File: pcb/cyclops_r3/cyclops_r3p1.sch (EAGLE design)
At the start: 59 parts, among them Q1 SUM11006, Q2 IRF510, U1 MCP4921, U2 317-N, U3 ADR03, U4 OP1177, U5 LM324N, U6 ZXTD45

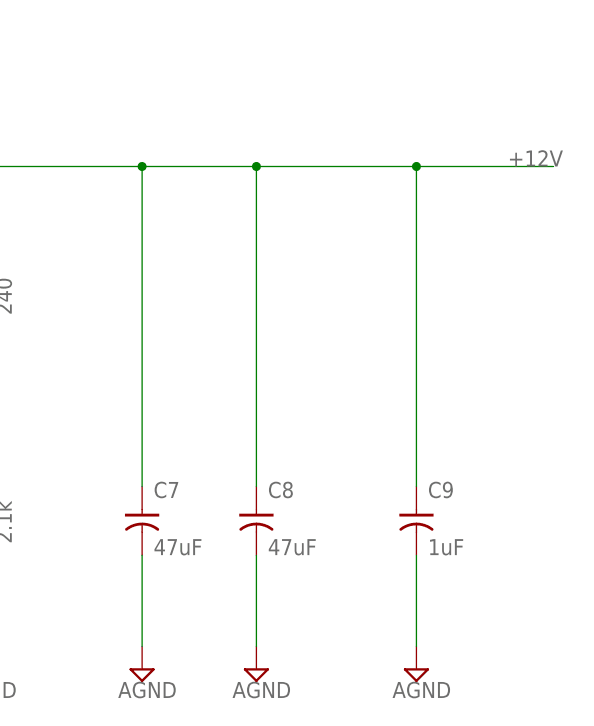
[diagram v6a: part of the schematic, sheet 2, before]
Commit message: Substantial changes to the layout of the analog frontend of the circuit.
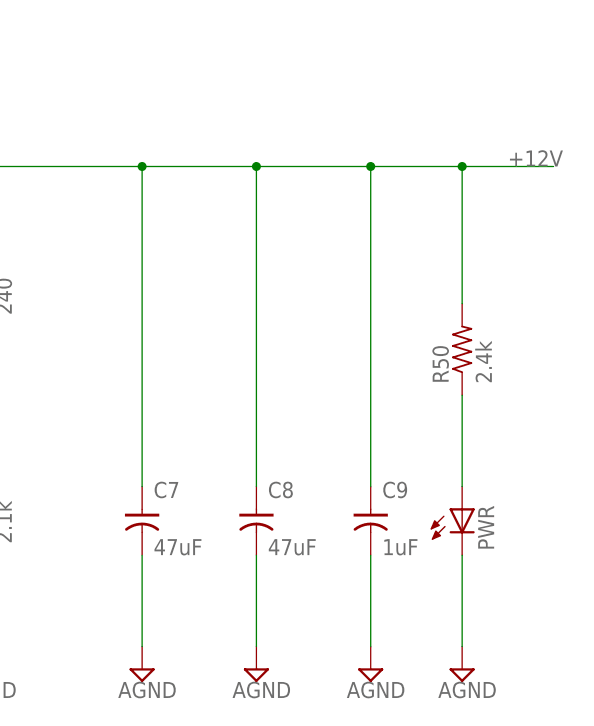
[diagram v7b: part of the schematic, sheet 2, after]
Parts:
- added PWR: (no value), cyclops:LEDYELLOW_0805
- added R50: 2.4k, cyclops:R_0603
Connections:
- net VREF2X renamed REFA2X
- new net N$3: PWR.A, R50.1
- new net REFA: C2.1, REF_ADJ.A, U1.REFA, U3.VOUT, U5A.+IN, VREF.TP
- net +12V: now also R50.2
- net GND: now also PWR.C
- net N$4: now also U5C.OUT; no longer U5A.OUT
- net N$8: now also U5A.-IN; no longer U5D.-IN
- net VFB: now also U5C.-IN; no longer U5A.-IN
- net VREF: now also U5D.-IN, U5D.OUT; no longer C2.1, REF_ADJ.A, U1.REFA, U3.VOUT, U5C.-IN, U5C.OUT, U5D.+IN, VREF.TP
- net VREFA2X: now also U5A.OUT; no longer U5D.OUT
- net _VREF: now also U5D.+IN; no longer U5A.+IN
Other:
- moved on the sheet: C9, U5A, U5C, U5D
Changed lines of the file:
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@@
 <part name="VBIAS" library="cyclops" deviceset="TP" device="TP08R"/>
 <part name="VGATE" library="cyclops" deviceset="TP" device="TP08R"/>
+<part name="R50" library="cyclops" deviceset="R" device="_0603" value="2.4k"/>
+<part name="PWR" library="cyclops" deviceset="LED" device="_0805" technology="YELLOW"/>
+<part name="SUPPLY40" library="supply2" deviceset="AGND" device=""/>
 </parts>
 <sheets>
@@
 </segment>
 </net>
-<net name="VREF" class="0">
-<segment>
-<pinref part="I/O_BLOCK" gate="G$1" pin="6"/>
-<wire x1="43.18" y1="-30.48" x2="68.58" y2="-30.48" width="0.1524" layer="91"/>
-<label x="50.8" y="-30.48" size="1.778" layer="95"/>
-</segment>
+<net name="REFA" class="0">
 <segment>
 <pinref part="U1" gate="G$1" pin="REFA"/>
@@
 </segment>
 </net>
-<net name="VREF2X" class="0">
+<net name="REFA2X" class="0">
 <segment>
 <pinref part="S3" gate="G$1" pin="3"/>
 <wire x1="119.38" y1="-27.94" x2="104.14" y2="-27.94" width="0.1524" layer="91"/>
 <label x="104.14" y="-27.94" size="1.778" layer="95"/>
+</segment>
+</net>
+<net name="VREF" class="0">
+<segment>
+<pinref part="I/O_BLOCK" gate="G$1" pin="6"/>
+<wire x1="43.18" y1="-30.48" x2="68.58" y2="-30.48" width="0.1524" layer="91"/>
+<label x="50.8" y="-30.48" size="1.778" layer="95"/>
 </segment>
 </net>
@@
 <instance part="SUPPLY8" gate="G$1" x="33.02" y="-58.42"/>
 <instance part="SUPPLY9" gate="G$1" x="86.36" y="-58.42"/>
-<instance part="SUPPLY10" gate="G$1" x="104.14" y="-58.42"/>
+<instance part="SUPPLY10" gate="G$1" x="99.06" y="-58.42"/>
 <instance part="C5" gate="C" x="12.7" y="-43.18"/>
 <instance part="C6" gate="C" x="33.02" y="-43.18"/>
-<instance part="C9" gate="C" x="104.14" y="-43.18"/>
+<instance part="C9" gate="C" x="99.06" y="-43.18"/>
 <instance part="C8" gate="C" x="86.36" y="-43.18"/>
 <instance part="SUPPLY11" gate="G$1" x="12.7" y="-58.42"/>
@@
 <instance part="C7" gate="C" x="73.66" y="-43.18"/>
 <instance part="SUPPLY31" gate="G$1" x="73.66" y="-58.42"/>
+<instance part="R50" gate="R" x="109.22" y="-22.86" rot="R90"/>
+<instance part="PWR" gate="G$1" x="109.22" y="-40.64"/>
+<instance part="SUPPLY40" gate="G$1" x="109.22" y="-58.42"/>
 </instances>
 <busses>
@@
 <wire x1="55.88" y1="-2.54" x2="73.66" y2="-2.54" width="0.1524" layer="91"/>
 <wire x1="73.66" y1="-2.54" x2="86.36" y2="-2.54" width="0.1524" layer="91"/>
-<wire x1="86.36" y1="-2.54" x2="104.14" y2="-2.54" width="0.1524" layer="91"/>
-<wire x1="104.14" y1="-2.54" x2="119.38" y2="-2.54" width="0.1524" layer="91"/>
+<wire x1="86.36" y1="-2.54" x2="99.06" y2="-2.54" width="0.1524" layer="91"/>
+<wire x1="99.06" y1="-2.54" x2="109.22" y2="-2.54" width="0.1524" layer="91"/>
+<wire x1="109.22" y1="-2.54" x2="119.38" y2="-2.54" width="0.1524" layer="91"/>
 <wire x1="38.1" y1="10.16" x2="55.88" y2="10.16" width="0.1524" layer="91"/>
 <wire x1="55.88" y1="10.16" x2="55.88" y2="-2.54" width="0.1524" layer="91"/>
@@
 <junction x="86.36" y="-2.54"/>
 <pinref part="C9" gate="C" pin="+"/>
-<wire x1="104.14" y1="-38.1" x2="104.14" y2="-2.54" width="0.1524" layer="91"/>
-<junction x="104.14" y="-2.54"/>
+<wire x1="99.06" y1="-38.1" x2="99.06" y2="-2.54" width="0.1524" layer="91"/>
+<junction x="99.06" y="-2.54"/>
 <label x="114.3" y="-2.54" size="1.778" layer="95"/>
 <pinref part="C7" gate="C" pin="+"/>
 <wire x1="73.66" y1="-38.1" x2="73.66" y2="-2.54" width="0.1524" layer="91"/>
 <junction x="73.66" y="-2.54"/>
+<pinref part="R50" gate="R" pin="2"/>
+<wire x1="109.22" y1="-17.78" x2="109.22" y2="-2.54" width="0.1524" layer="91"/>
+<junction x="109.22" y="-2.54"/>
 </segment>
 </net>
@@
 <pinref part="C9" gate="C" pin="-"/>
 <pinref part="SUPPLY10" gate="G$1" pin="AGND"/>
-<wire x1="104.14" y1="-45.72" x2="104.14" y2="-55.88" width="0.1524" layer="91"/>
+<wire x1="99.06" y1="-45.72" x2="99.06" y2="-55.88" width="0.1524" layer="91"/>
 </segment>
 <segment>
@@
 <wire x1="73.66" y1="-45.72" x2="73.66" y2="-55.88" width="0.1524" layer="91"/>
 <pinref part="SUPPLY31" gate="G$1" pin="AGND"/>
+</segment>
+<segment>
+<pinref part="PWR" gate="G$1" pin="C"/>
+<pinref part="SUPPLY40" gate="G$1" pin="AGND"/>
+<wire x1="109.22" y1="-45.72" x2="109.22" y2="-55.88" width="0.1524" layer="91"/>
 </segment>
 </net>
@@
 <wire x1="-10.16" y1="-15.24" x2="-10.16" y2="-2.54" width="0.1524" layer="91"/>
 <junction x="-10.16" y="-2.54"/>
+</segment>
+</net>
+<net name="N$3" class="0">
+<segment>
+<pinref part="R50" gate="R" pin="1"/>
+<wire x1="109.22" y1="-27.94" x2="109.22" y2="-38.1" width="0.1524" layer="91"/>
+<pinref part="PWR" gate="G$1" pin="A"/>
 </segment>
 </net>
@@
 </segment>
 </net>
-<net name="VREF" class="0">
+<net name="REFA" class="0">
 <segment>
 <wire x1="17.78" y1="2.54" x2="35.56" y2="2.54" width="0.1524" layer="91"/>
@@
 </plain>
 <instances>
-<instance part="U5" gate="A" x="27.94" y="83.82"/>
+<instance part="U5" gate="C" x="27.94" y="83.82"/>
 <instance part="U5" gate="B" x="27.94" y="22.86" rot="MR0"/>
-<instance part="U5" gate="C" x="-45.72" y="139.7" rot="MR0"/>
+<instance part="U5" gate="D" x="-45.72" y="139.7" rot="MR0"/>
 <instance part="U5" gate="P" x="27.94" y="83.82"/>
 <instance part="CTL_K" gate="1" x="-55.88" y="81.28" rot="MR90"/>
@@
 <instance part="R12" gate="R" x="134.62" y="71.12" rot="R90"/>
 <instance part="SUPPLY1" gate="G$1" x="134.62" y="45.72"/>
-<instance part="U5" gate="D" x="-53.34" y="-5.08"/>
+<instance part="U5" gate="A" x="-53.34" y="-5.08"/>
 <instance part="R13" gate="R" x="-40.64" y="-27.94" rot="R270"/>
 <instance part="R14" gate="R" x="-53.34" y="-15.24" rot="R180"/>
@@
 <wire x1="12.7" y1="81.28" x2="20.32" y2="81.28" width="0.1524" layer="91"/>
 <wire x1="12.7" y1="63.5" x2="12.7" y2="81.28" width="0.1524" layer="91"/>
-<pinref part="U5" gate="A" pin="-IN"/>
+<pinref part="U5" gate="C" pin="-IN"/>
 <pinref part="S4" gate="G$1" pin="2"/>
 </segment>
@@
 </segment>
 </net>
-<net name="VREF" class="0">
-<segment>
-<wire x1="-38.1" y1="137.16" x2="-38.1" y2="129.54" width="0.1524" layer="91"/>
-<wire x1="-38.1" y1="129.54" x2="-58.42" y2="129.54" width="0.1524" layer="91"/>
-<pinref part="U5" gate="C" pin="-IN"/>
-<wire x1="-73.66" y1="139.7" x2="-58.42" y2="139.7" width="0.1524" layer="91"/>
-<wire x1="-58.42" y1="139.7" x2="-53.34" y2="139.7" width="0.1524" layer="91"/>
-<wire x1="-58.42" y1="129.54" x2="-58.42" y2="139.7" width="0.1524" layer="91"/>
-<junction x="-58.42" y="139.7"/>
-<pinref part="U5" gate="C" pin="OUT"/>
-<label x="-73.66" y="139.7" size="1.778" layer="95"/>
-</segment>
-<segment>
-<pinref part="U5" gate="D" pin="+IN"/>
+<net name="REFA" class="0">
+<segment>
+<pinref part="U5" gate="A" pin="+IN"/>
 <wire x1="-73.66" y1="-2.54" x2="-60.96" y2="-2.54" width="0.1524" layer="91"/>
 <label x="-73.66" y="-2.54" size="1.778" layer="95"/>
@@
 <net name="_VREF" class="0">
 <segment>
-<pinref part="U5" gate="A" pin="+IN"/>
+<pinref part="U5" gate="C" pin="+IN"/>
 <pinref part="D4" gate="G$1" pin="C"/>
 <pinref part="R7" gate="R" pin="2"/>
@@
 <wire x1="-10.16" y1="86.36" x2="-10.16" y2="93.98" width="0.1524" layer="91"/>
 <wire x1="-20.32" y1="142.24" x2="-20.32" y2="86.36" width="0.1524" layer="91"/>
-<pinref part="U5" gate="C" pin="+IN"/>
+<pinref part="U5" gate="D" pin="+IN"/>
 <wire x1="-38.1" y1="142.24" x2="-20.32" y2="142.24" width="0.1524" layer="91"/>
 <junction x="-20.32" y="86.36"/>
@@
 <segment>
 <wire x1="-40.64" y1="-15.24" x2="-40.64" y2="-5.08" width="0.1524" layer="91"/>
-<pinref part="U5" gate="D" pin="OUT"/>
+<pinref part="U5" gate="A" pin="OUT"/>
 <wire x1="-40.64" y1="-5.08" x2="-45.72" y2="-5.08" width="0.1524" layer="91"/>
 <wire x1="-40.64" y1="-5.08" x2="-30.48" y2="-5.08" width="0.1524" layer="91"/>
@@
 <segment>
 <wire x1="-66.04" y1="-7.62" x2="-66.04" y2="-15.24" width="0.1524" layer="91"/>
-<pinref part="U5" gate="D" pin="-IN"/>
+<pinref part="U5" gate="A" pin="-IN"/>
 <wire x1="-60.96" y1="-7.62" x2="-66.04" y2="-7.62" width="0.1524" layer="91"/>
 <pinref part="R14" gate="R" pin="2"/>
@@
 </segment>
 </net>
-<net name="VREF2X" class="0">
+<net name="REFA2X" class="0">
 <segment>
 <pinref part="R15" gate="R" pin="2"/>
@@
 <net name="N$4" class="0">
 <segment>
-<pinref part="U5" gate="A" pin="OUT"/>
+<pinref part="U5" gate="C" pin="OUT"/>
 <wire x1="35.56" y1="83.82" x2="43.18" y2="83.82" width="0.1524" layer="91"/>
 <wire x1="43.18" y1="83.82" x2="43.18" y2="124.46" width="0.1524" layer="91"/>
@@
 </segment>
 </net>
+<net name="VREF" class="0">
+<segment>
+<wire x1="-38.1" y1="137.16" x2="-38.1" y2="129.54" width="0.1524" layer="91"/>
+<wire x1="-38.1" y1="129.54" x2="-58.42" y2="129.54" width="0.1524" layer="91"/>
+<pinref part="U5" gate="D" pin="-IN"/>
+<wire x1="-73.66" y1="139.7" x2="-58.42" y2="139.7" width="0.1524" layer="91"/>
+<wire x1="-58.42" y1="139.7" x2="-53.34" y2="139.7" width="0.1524" layer="91"/>
+<wire x1="-58.42" y1="129.54" x2="-58.42" y2="139.7" width="0.1524" layer="91"/>
+<junction x="-58.42" y="139.7"/>
+<pinref part="U5" gate="D" pin="OUT"/>
+<label x="-73.66" y="139.7" size="1.778" layer="95"/>
+</segment>
+</net>

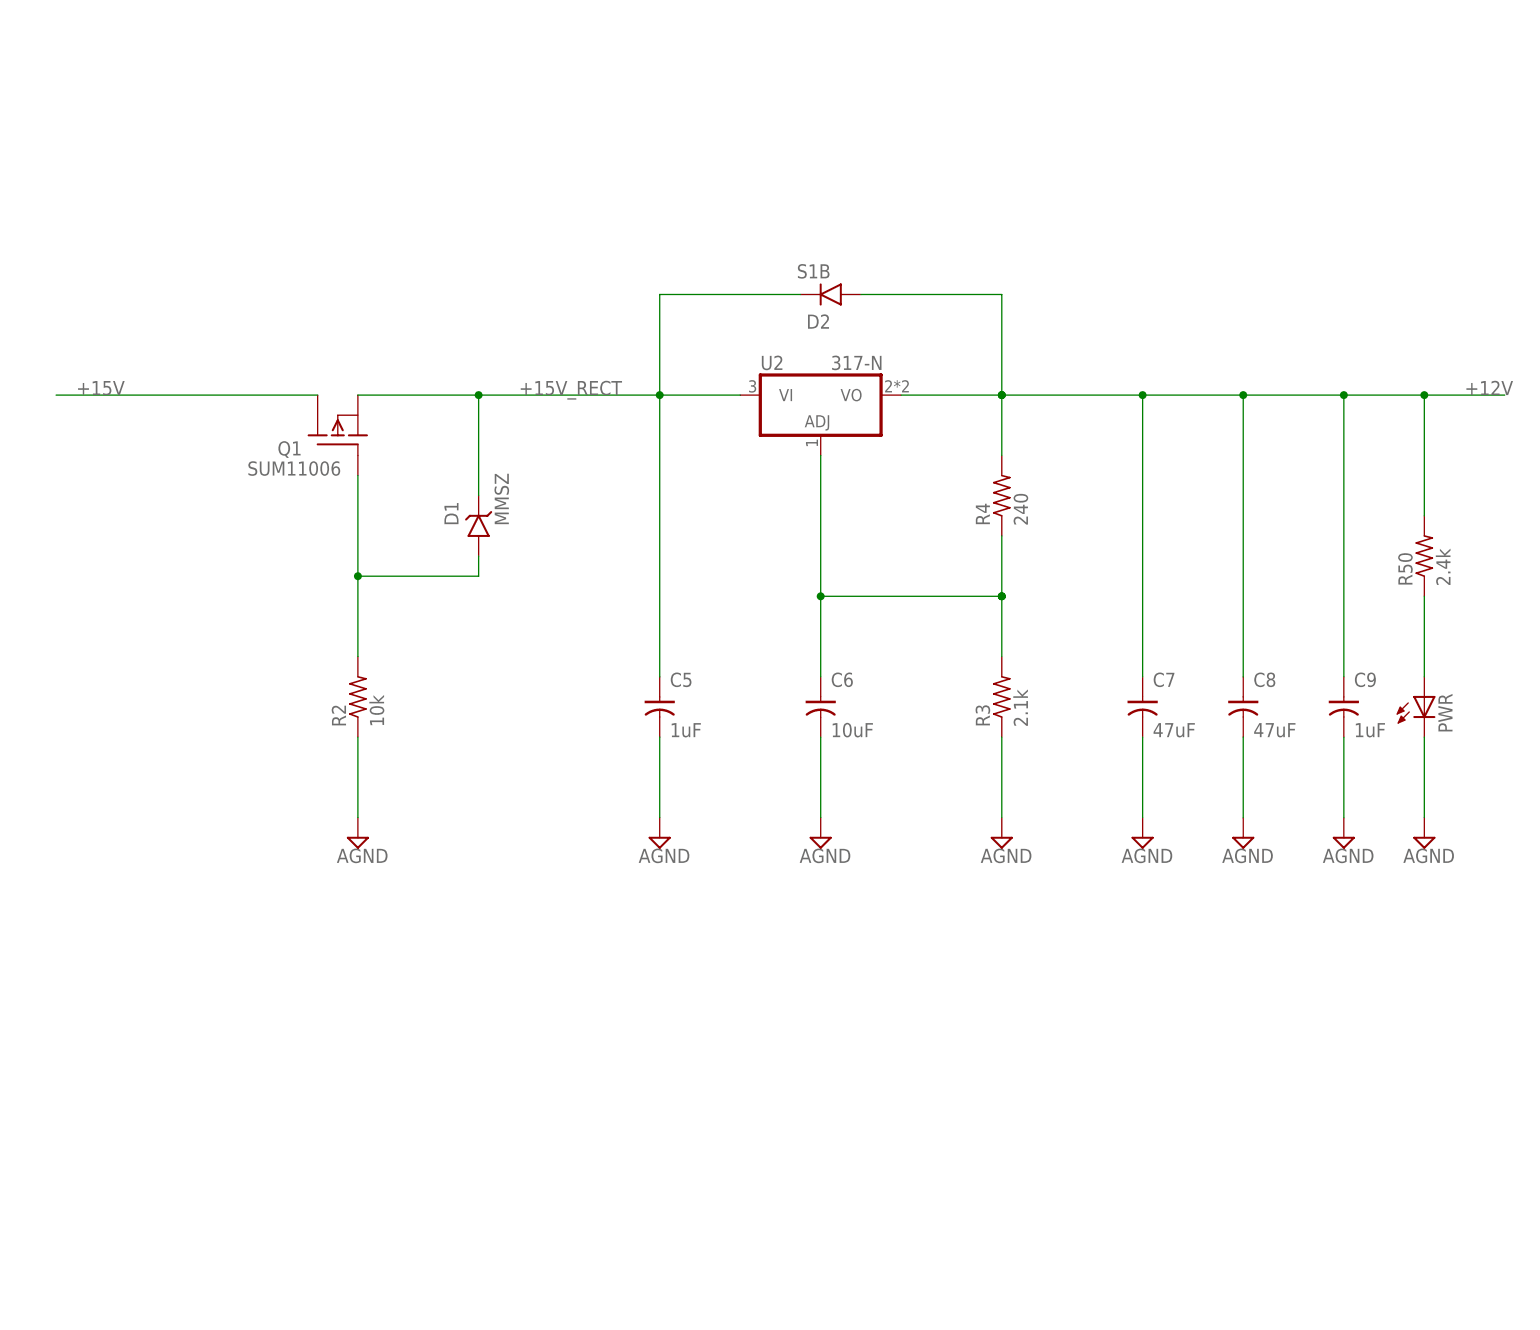
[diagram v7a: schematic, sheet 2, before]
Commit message: Added an overcurrent kill circuit. This needs to be tested. Also, a reset switch needs to be added.
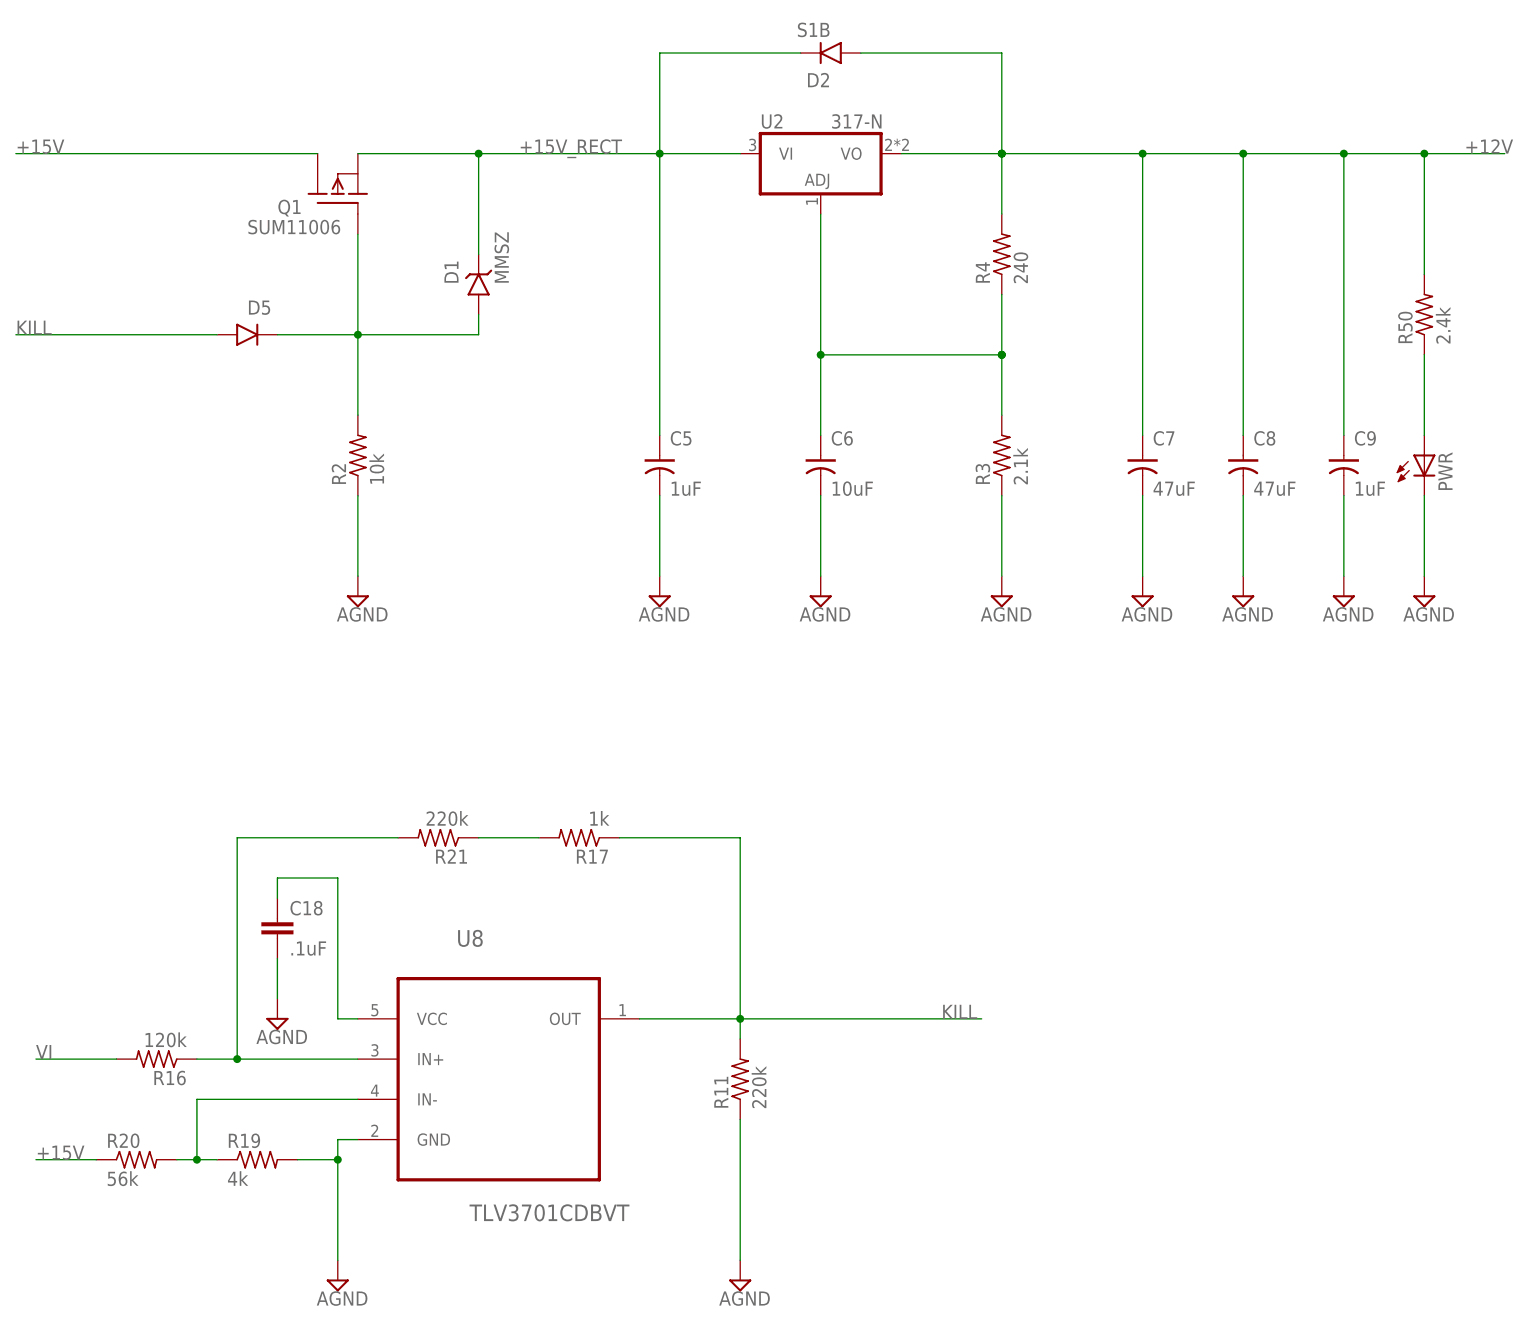
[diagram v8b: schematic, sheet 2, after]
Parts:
- added C18: .1uF, cyclops:C_0603
- added D5: (no value), cyclops:DIODESOD-323
- added R11, R21: 220k, cyclops:R_0603
- added R16: 120k, cyclops:R_0603
- added R17: 1k, cyclops:R_0603
- added R19: 4k, cyclops:R_0603
- added R20: 56k, cyclops:R_0603
- added U8: TLV3701CDBVT, ti-extended:TLV3701CDBVT
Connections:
- new net KILL: D5.A, R11.2, R17.1, U8.OUT
- new net N$14: R16.1, R21.2, U8.IN+
- new net N$5: R19.1, R20.2, U8.IN-
- new net N$9: R17.2, R21.1
- net +15V: now also C18.1, R20.1, U8.VCC
- net GND: now also C18.2, R11.1, R19.2, U8.GND
- net N$18: now also D5.C
- net VI: now also R16.2
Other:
- moved on the sheet: C5, C6, C7, C8, C9, D1, D2, PWR, Q1, R2, R3, R4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
